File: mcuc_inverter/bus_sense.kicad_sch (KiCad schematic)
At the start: 0 parts

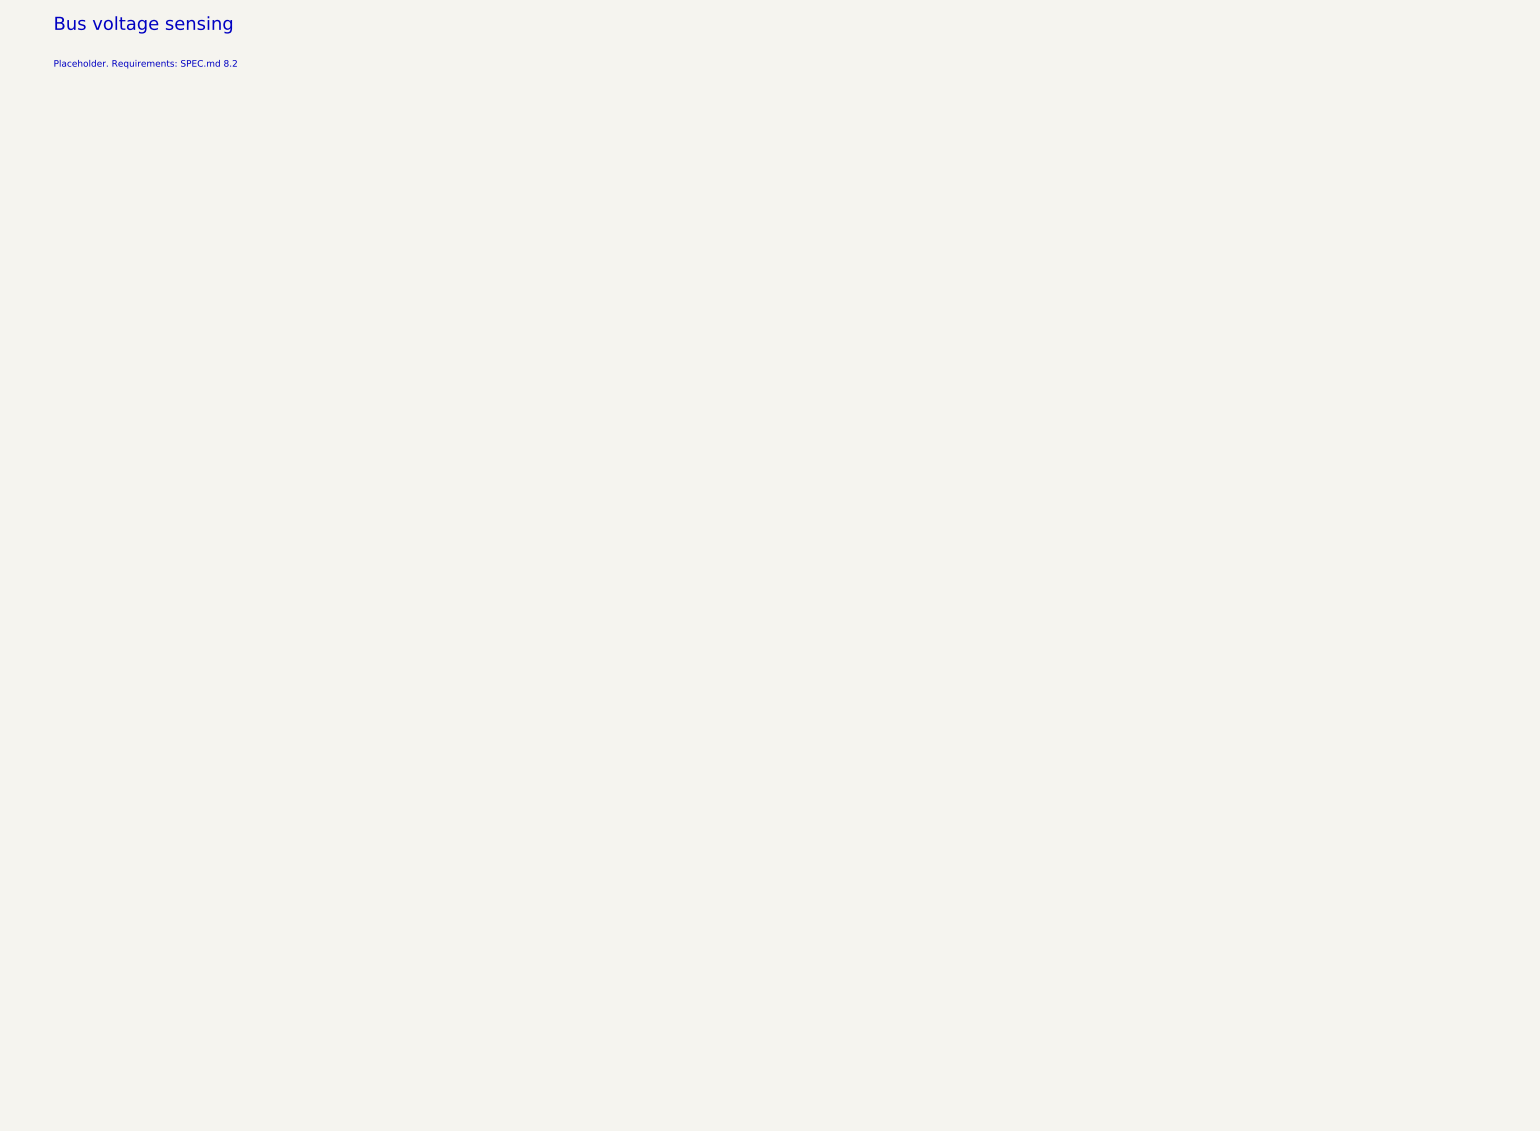
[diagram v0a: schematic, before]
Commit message: Capture bus_sense, temp_sense, comms: all 11 sheets now live
bus_sense: 4x750k + 12.0k string (strict series, 124.5 V/part) into
AMC1311BDWV (pinout verified vs SBAS786C; B-grade 3.0-5.5 V VDD1 is
load-bearing per D022; no input clamp diodes per TI 9.3), HV-side
3.3 V from MCP1804T-3302 (2-28 V in, stocked - no TBV needed) off
the VGD_LS rail, diff-to-SE gain 0.75: V_BUS = 2.988 mV/V, 500 V ->
1.494 V, saturates ~1.50 V, always < 3.3 V.

temp_sense: coldplate NTC channel (B57861S off-board via J1101),
board NTC (NCU18 successor), 6x DNP TS provision pads onto the
module TS pins with D022 rationale quoted on-sheet.

comms: ISO1042DWR isolated CAN (VCC2 pins 11/16 tied - datasheet
requirement), split termination + TVS added (legacy sheet flagged
its own missing protection), USB-C + USBLC6 to MCU 70/71, keyed SWD,
status LEDs, I/O connectors. CAN_TX/RX verified onto MCU pins 96/95;
CONTACTOR_P/N resolve onto the precharge coil driver.

ERC 0 errors; netlist machine-checks per sheet; key cross-sheet
nets independently re-verified. 11 of 11 sheets captured.

Co-Authored-By: Claude Fable 5 <noreply@anthropic.com>
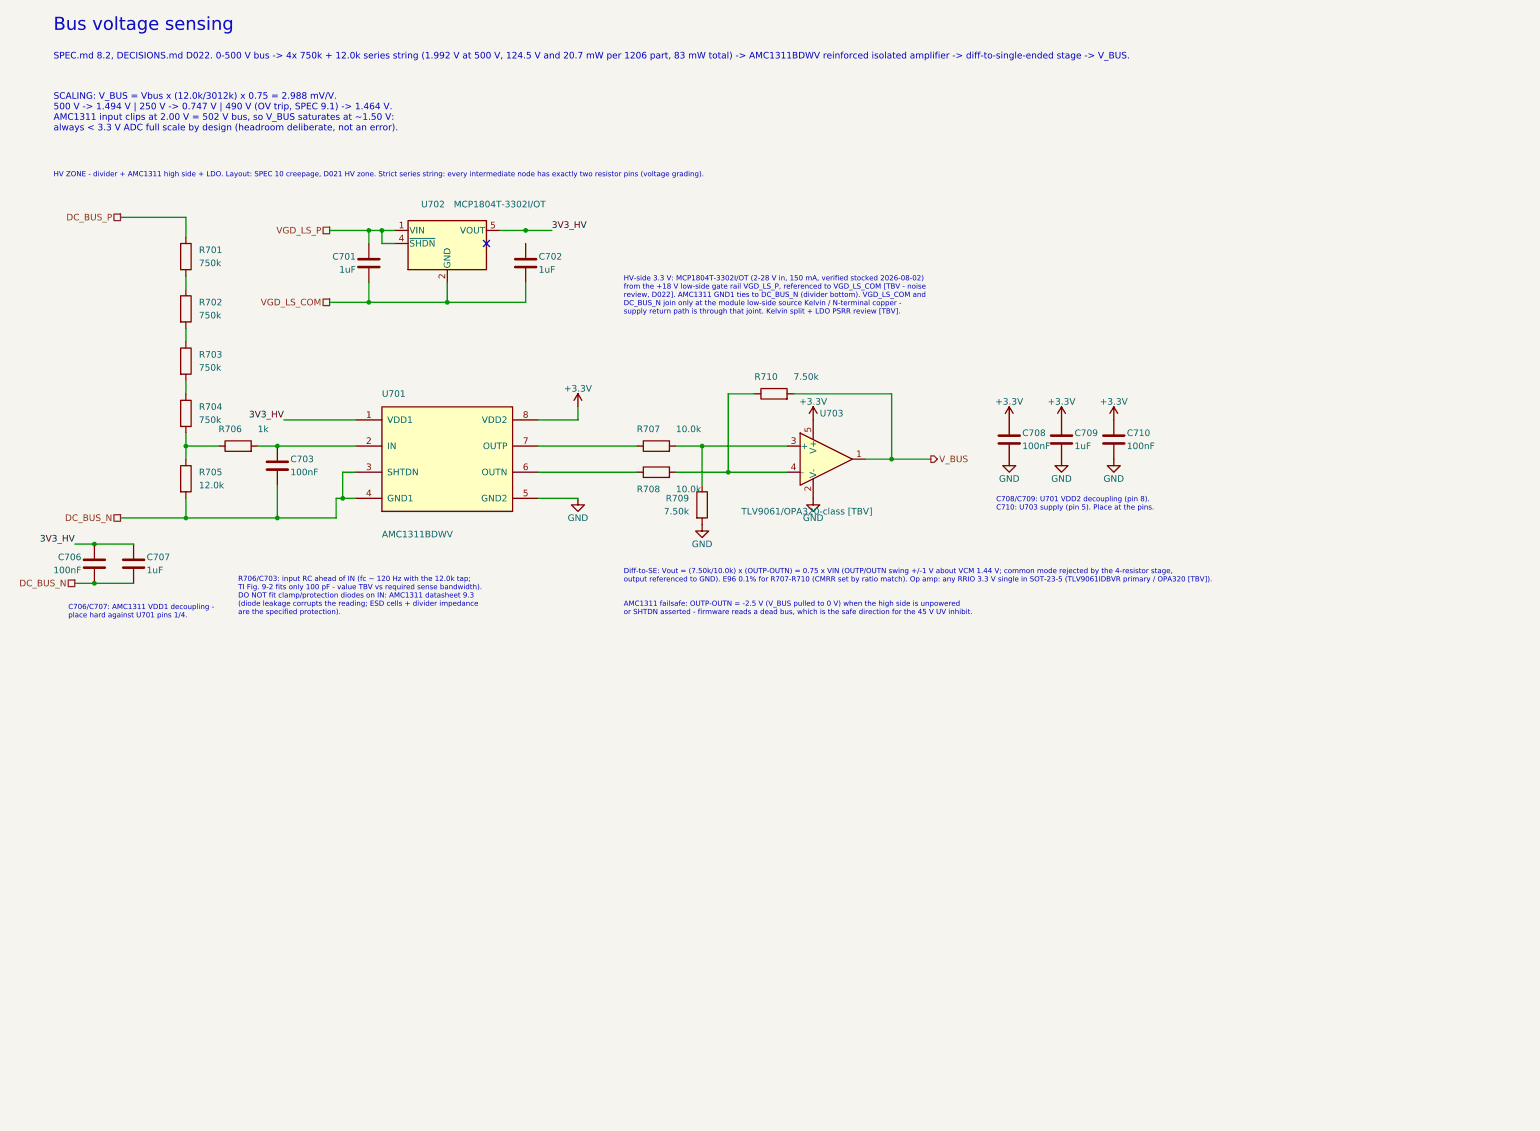
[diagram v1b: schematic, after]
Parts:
- added C701, C702, C707, C709: 1uF, Capacitor_SMD:C_0603_1608Metric, symbol Device:C
- added C703, C706, C708, C710: 100nF, Capacitor_SMD:C_0603_1608Metric, symbol Device:C
- added R701, R702, R703, R704: 750k, Resistor_SMD:R_1206_3216Metric, symbol Device:R
- added R705: 12.0k, Resistor_SMD:R_0603_1608Metric, symbol Device:R
- added R706: 1k, Resistor_SMD:R_0603_1608Metric, symbol Device:R
- added R707, R708: 10.0k, Resistor_SMD:R_0603_1608Metric, symbol Device:R
- added R709, R710: 7.50k, Resistor_SMD:R_0603_1608Metric, symbol Device:R
- added U701: AMC1311BDWV, Package_SO:SOIC-8_7.5x5.85mm_P1.27mm, symbol mcuc:AMC1311BDWV
- added U702: MCP1804T-3302I/OT, Package_TO_SOT_SMD:SOT-23-5, symbol Regulator_Linear:MCP1804x-3302xOT
- added U703: TLV9061/OPA320-class [TBV], Package_TO_SOT_SMD:SOT-23-5, symbol Amplifier_Operational:TLV9061xDBV
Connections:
- new net: R704.2, R705.1, R706.1
- new net: R707.2, R709.1, U703.3 (+)
- new net: C703.1, R706.2, U701.2 (IN)
- new net: R708.1, U701.6 (OUTN)
- new net: R707.1, U701.7 (OUTP)
- new net: R703.2, R704.1
- new net: R701.2, R702.1
- new net: R702.2, R703.1
- new net: R708.2, R710.1, U703.4 (-)
- new net +3.3V: C708.1, C709.1, C710.1, U701.8 (VDD2), U703.5 (V+)
- new net 3V3_HV: C706.1, C707.1, U701.1 (VDD1), U702.5 (VOUT)
- new net DC_BUS_N: C703.2, C706.2, C707.2, R705.2, U701.3 (SHTDN), U701.4 (GND1)
- new net DC_BUS_P: R701.1
- new net GND: C708.2, C709.2, C710.2, R709.2, U701.5 (GND2), U703.2 (V-)
- new net VGD_LS_COM: C701.2, C702.2, U702.2 (GND)
- new net VGD_LS_P: C701.1, U702.1 (VIN), U702.4 (~{SHDN})
- new net V_BUS: R710.2, U703.1
- no-connect marks 0 -> 1
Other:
- note added: "AMC1311 failsafe: OUTP-OUTN = -2.5 V (V_BUS pulled to 0 V) when the high side is unpowered or SHTDN asserted - firmware reads a dead bus, which is the safe direction for the 45 V UV inhibit."
- note added: "C706/C707: AMC1311 VDD1 decoupling - place hard against U701 pins 1/4."
- note added: "C708/C709: U701 VDD2 decoupling (pin 8). C710: U703 supply (pin 5). Place at the pins."
- note added: "Diff-to-SE: Vout = (7.50k/10.0k) x (OUTP-OUTN) = 0.75 x VIN (OUTP/OUTN swing +/-1 V about VCM 1.44 V; common mode rejected by the 4-resistor stage, output referenced to GND). E96 0.1% for R707-R710 (CMRR set by ratio match). Op amp: any RRIO 3.3 V single in SOT-23-5 (TLV9061IDBVR primary / OPA320 [TBV])."
- note added: "HV ZONE - divider + AMC1311 high side + LDO. Layout: SPEC 10 creepage, D021 HV zone. Strict series string: every intermediate node has exactly two resistor pins (voltage grading)."
- note added: "HV-side 3.3 V: MCP1804T-3302I/OT (2-28 V in, 150 mA, verified stocked 2026-08-02) from the +18 V low-side gate rail VGD_LS_P, referenced to VGD_LS_COM [TBV - noise review, D022]. AMC1311 GND1 ties to DC_BUS_N (divider bottom). VGD_LS_COM and DC_BUS_N join only at the module low-side source Kelvin / N-terminal copper - supply return path is through that joint. Kelvin split + LDO PSRR review [TBV]."
- note added: "R706/C703: input RC ahead of IN (fc ~ 120 Hz with the 12.0k tap; TI Fig. 9-2 fits only 100 pF - value TBV vs required sense bandwidth). DO NOT fit clamp/protection diodes on IN: AMC1311 datasheet 9.3 (diode leakage corrupts the reading; ESD cells + divider impedance are the specified protection)."
- note added: "SCALING: V_BUS = Vbus x (12.0k/3012k) x 0.75 = 2.988 mV/V. 500 V -> 1.494 V | 250 V -> 0.747 V | 490 V (OV trip, SPEC 9.1) -> 1.464 V. AMC1311 input clips at 2.00 V = 502 V bus, so V_BUS saturates at ~1.50 V: always < 3.3 V ADC full scale by design (headroom deliberate, not an error)."
- note added: "SPEC.md 8.2, DECISIONS.md D022. 0-500 V bus -> 4x 750k + 12.0k series string (1.992 V at 500 V, 124.5 V and 20.7 mW per 1206 part, 83 mW total) -> AMC1311BDWV reinforced isolated amplifier -> diff-to-single-ended stage -> V_BUS."
- note removed: "Placeholder. Requirements: SPEC.md 8.2"
